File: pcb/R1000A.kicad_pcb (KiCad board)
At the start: 4 copper layers, 175 x 65.5 mm, 120 parts, among them J01 PCIESOCKET-X1, J02 PCIESOCKET-X1, J03 PCIESOCKET-X1, J04 PCIESOCKET-X1, J05 PCIESOCKET-X1, J06 PCIESOCKET-X1, J07 PCIESOCKET-X1, J08 PCIESOCKET-X1, J09 PCIESOCKET-X1, J10 PCIESOCKET-X1, J11 PCIESOCKET-X1, J12 PCIESOCKET-X1, J13 PCIESOCKET-X1, J14 PCIESOCKET-X1, J15 PCIESOCKET-X1, J17 USB_B_RECEPTACLE, J2 CONN127P-02X05, J25 SOCKET420P-02X04-CPU, J27 CONN500P-01X04, J31 USB_A_RECEPTACLE_2, J80 SOCKET254P-01X02, J81 SOCKET254P-01X02, J82 SOCKET254P-01X02, J83 CONN_01X03, Q1 DMG2305UX-7, Q2 PSMN1R2-30YLC, Q3 Q_PNP_BEC, Q4 Q_NPN_BEC, U1 LPC1769FBD100,551, U2 AP3418, U3 BD9E302EFJ-E2, U4 INA3221AIRGVR, U5 LM5060MM/NOPB, Y1 XTAL4_12MHz

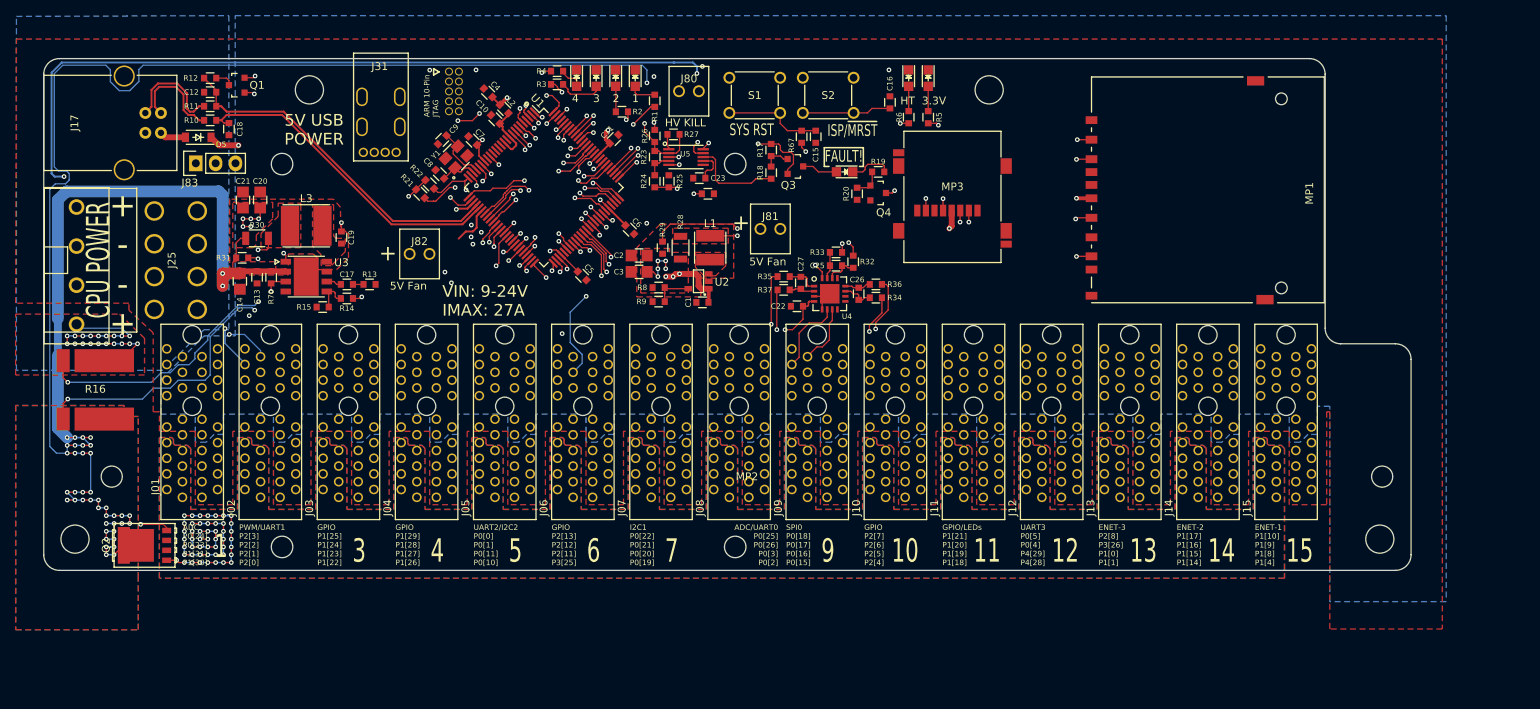
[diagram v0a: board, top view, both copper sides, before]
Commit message: added fiducials and re-laid ground and high tension planes
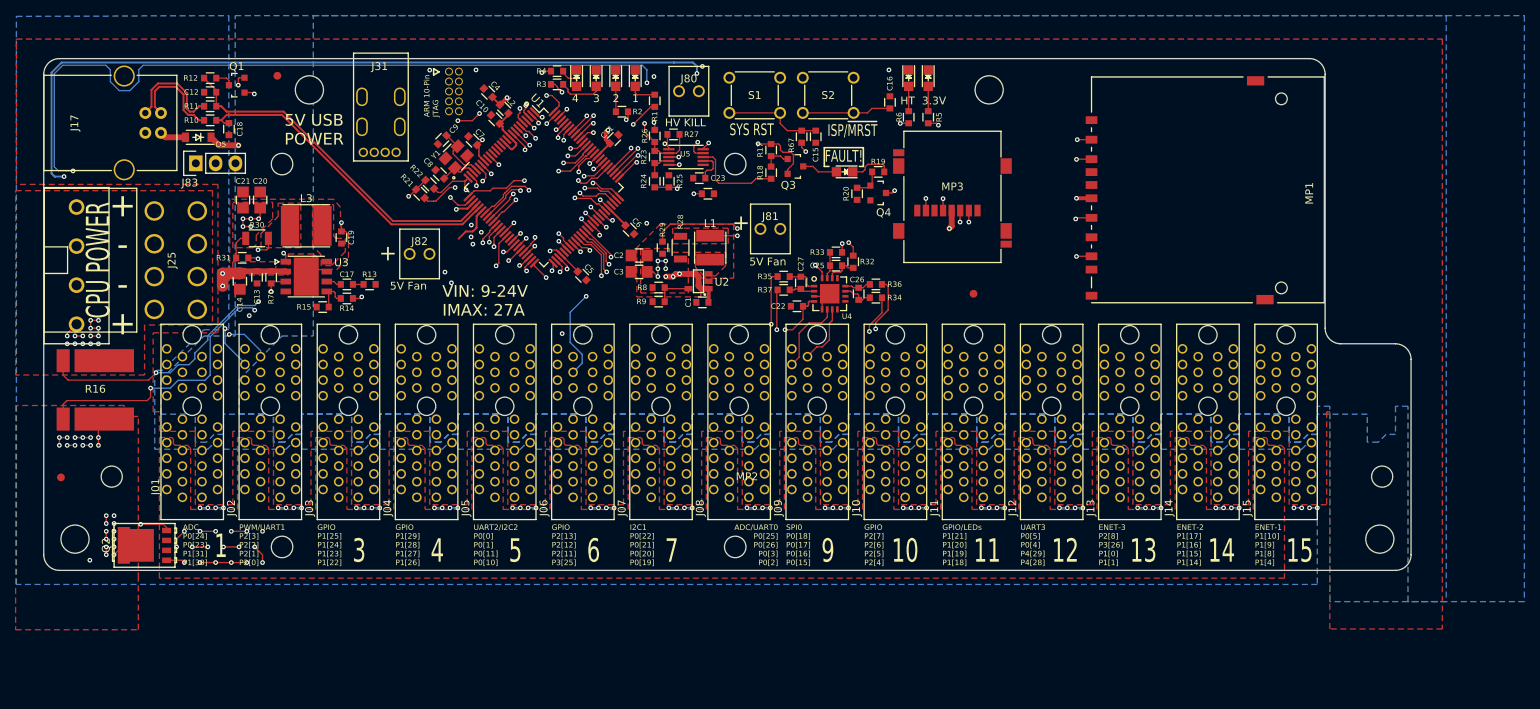
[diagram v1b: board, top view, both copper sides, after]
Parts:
- added FID1: FIDTOP001, Main:FIDTOP001, F.Cu at (80.9, 75.7)
- added FID2: FIDTOP001, Main:FIDTOP001, F.Cu at (53.2, 127.1)
- added FID3: FIDTOP001, Main:FIDTOP001, F.Cu at (170.0, 103.6)
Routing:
- net GND: track 15.0 -> 159.5 mm, vias 0 -> 60
- net PFET_D: track 306.1 -> 248.2 mm, vias 44 -> 30
- net HT_IN: track 32.2 -> 19.4 mm, vias 19 -> 14
- net HT: track 259.4 -> 247.1 mm, vias 54 -> 22
- net /PowerMonitor/IIN-: track 120.9 -> 121.5 mm
- net /PowerMonitor/LM5060_GATE: track 189.1 -> 189.3 mm, vias 4 -> 5
- added copper zone on B.Cu, net GND
- added copper zone on In1.Cu, net HT_IN
- removed copper zone on B.Cu, net HT
- removed copper zone on In2.Cu, net HT
- removed copper zone on B.Cu, net HT_IN
- removed copper zone on In2.Cu, net HT_IN
- removed copper zone on B.Cu, net PFET_D
- removed copper zone on In2.Cu, net PFET_D

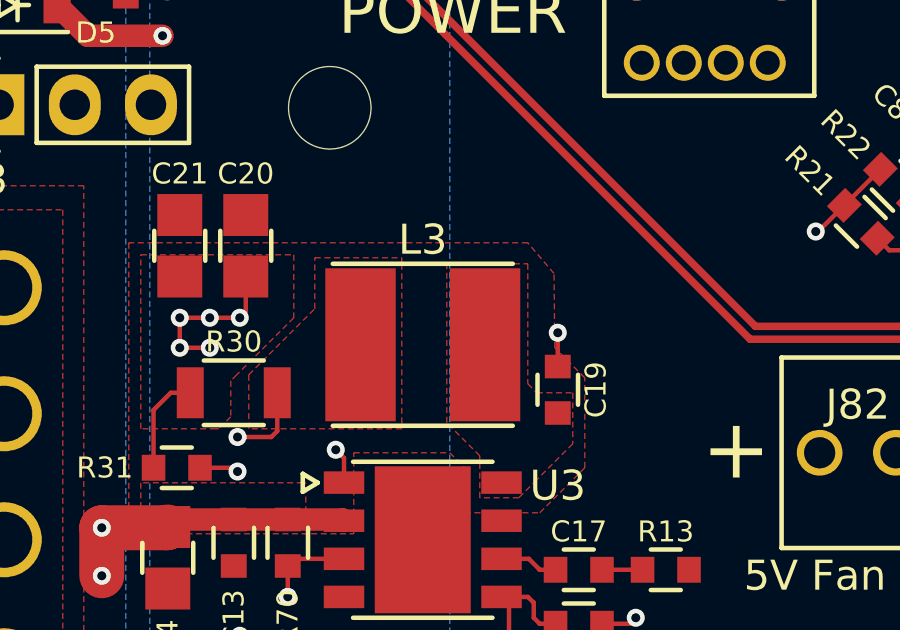
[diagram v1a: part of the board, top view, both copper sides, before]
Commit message: fixed dfm orientation for L3
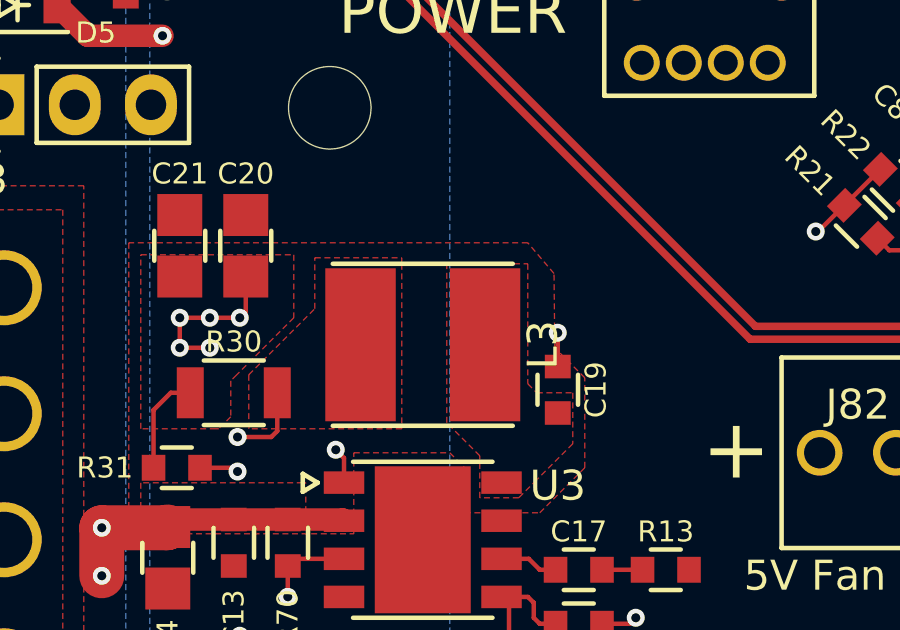
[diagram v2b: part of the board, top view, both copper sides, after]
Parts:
- turned L3 to 270 degrees
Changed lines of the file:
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@@
     (links 716)
     (no_connects 0)
-    (area 50.924999 73.424999 226.075001 139.075001)
+    (area 47.4 63.678571 240.500001 147.400001)
     (thickness 1.6)
     (drawings 71)
@@
   (page A4)
   (layers
-    (0 F.Cu signal hide)
+    (0 F.Cu signal)
     (1 In1.Cu signal hide)
-    (2 In2.Cu signal)
+    (2 In2.Cu signal hide)
     (31 B.Cu signal hide)
     (32 B.Adhes user)
@@
     )
   )
-  (module Main:INDP600600X420 (layer F.Cu)
-    (at 84.6 94.9 180)
-    (fp_text reference L3 (at 0 3.5 180) (layer F.SilkS)
-      (effects (font (size 1 1) (thickness 0.15)))
-    )
-    (fp_text value INDUCTOR_SRN6045TA-4R7M (at 0 -0.5 180) (layer F.Fab) hide
-      (effects (font (size 0.127 0.127) (thickness 0.03)))
-    )
-    (fp_line (start 3.3 2.8) (end -3.3 2.8) (layer F.CrtYd) (width 0.1524))
-    (fp_line (start -3.3 2.8) (end -3.3 -2.8) (layer F.CrtYd) (width 0.1524))
-    (fp_line (start -3.3 -2.8) (end 3.3 -2.8) (layer F.CrtYd) (width 0.1524))
-    (fp_line (start 3.3 -2.8) (end 3.3 2.8) (layer F.CrtYd) (width 0.1524))
-    (fp_line (start 3 2.7) (end -3 2.7) (layer F.SilkS) (width 0.1524))
-    (fp_line (start 3 -2.7) (end -3 -2.7) (layer F.SilkS) (width 0.1524))
-    (pad 1 smd rect (at -2.075 0 180) (size 2.35 5.1) (layers F.Cu F.Paste F.Mask)
-      (net 89 /Power/SW5V0))
-    (pad 2 smd rect (at 2.075 0 180) (size 2.35 5.1) (layers F.Cu F.Paste F.Mask)
-      (net 124 5V0+))
-    (model main.3dshapes/INDP600600X420.wrl
-      (at (xyz 0 0 0))
-      (scale (xyz 1 1 1))
-      (rotate (xyz 0 0 0))
-    )
-  )
   (module Main:CONN_SCHD3A0100 (layer F.Cu)
     (at 167.3 82.8)
@@
       (solder_mask_margin 0.77) (clearance 0.77))
   )
+  (module Main:INDP600600X420 (layer F.Cu)
+    (at 84.6 94.9 270)
+    (fp_text reference L3 (at 0 -4 270) (layer F.SilkS)
+      (effects (font (size 1 1) (thickness 0.15)))
+    )
+    (fp_text value INDUCTOR_SRN6045TA-4R7M (at 0 -0.5 270) (layer F.Fab) hide
+      (effects (font (size 0.127 0.127) (thickness 0.03)))
+    )
+    (fp_line (start 2.8 3.3) (end 2.8 -3.3) (layer F.CrtYd) (width 0.1524))
+    (fp_line (start 2.8 -3.3) (end -2.8 -3.3) (layer F.CrtYd) (width 0.1524))
+    (fp_line (start -2.8 -3.3) (end -2.8 3.3) (layer F.CrtYd) (width 0.1524))
+    (fp_line (start -2.8 3.3) (end 2.8 3.3) (layer F.CrtYd) (width 0.1524))
+    (fp_line (start 2.7 3) (end 2.7 -3) (layer F.SilkS) (width 0.1524))
+    (fp_line (start -2.7 3) (end -2.7 -3) (layer F.SilkS) (width 0.1524))
+    (pad 1 smd rect (at 0 -2.075 270) (size 5.1 2.35) (layers F.Cu F.Paste F.Mask)
+      (net 89 /Power/SW5V0))
+    (pad 2 smd rect (at 0 2.075 270) (size 5.1 2.35) (layers F.Cu F.Paste F.Mask)
+      (net 124 5V0+))
+    (model main.3dshapes/INDP600600X420.wrl
+      (at (xyz 0 0 0))
+      (scale (xyz 1 1 1))
+      (rotate (xyz 0 0 0))
+    )
+  )
   (gr_text "HV KILL" (at 130.5 81.7) (layer F.SilkS)

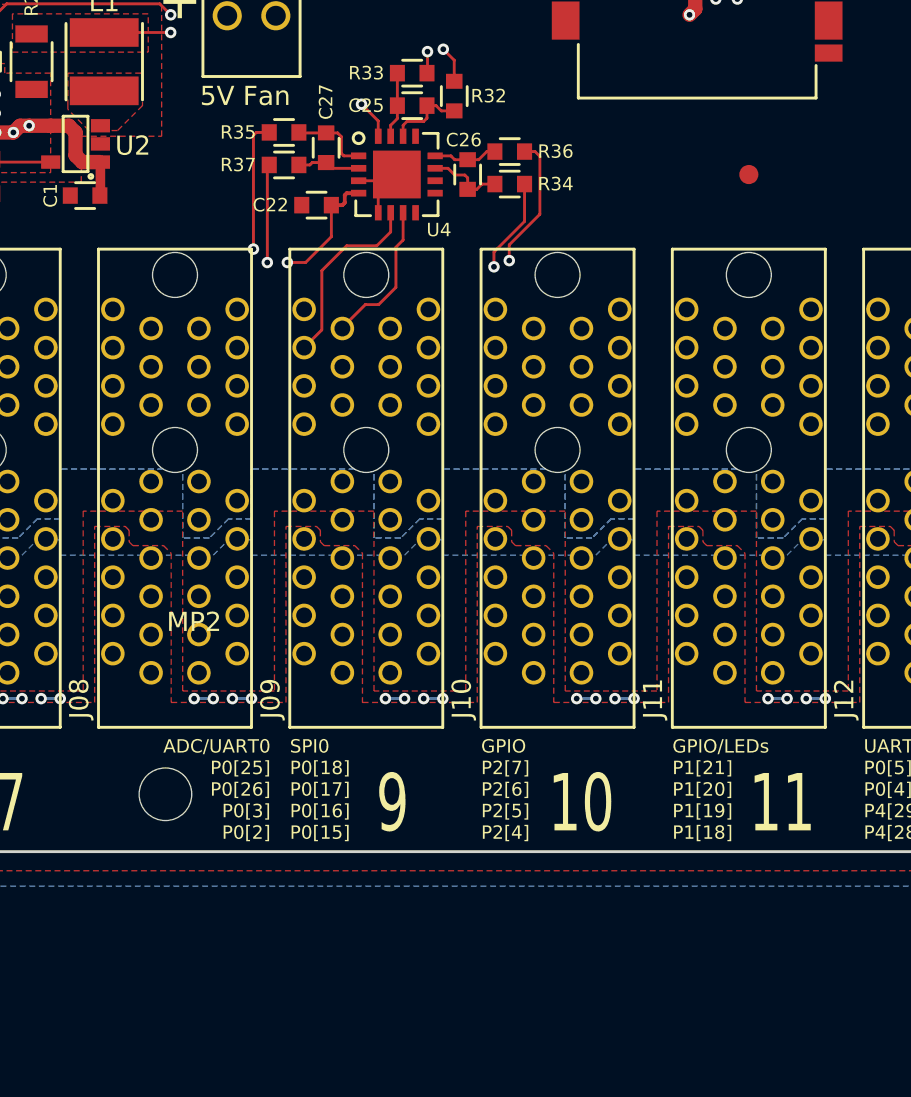
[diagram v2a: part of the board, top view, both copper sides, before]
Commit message: wip, added eeprom and test point for write protecting ROM during normal operation
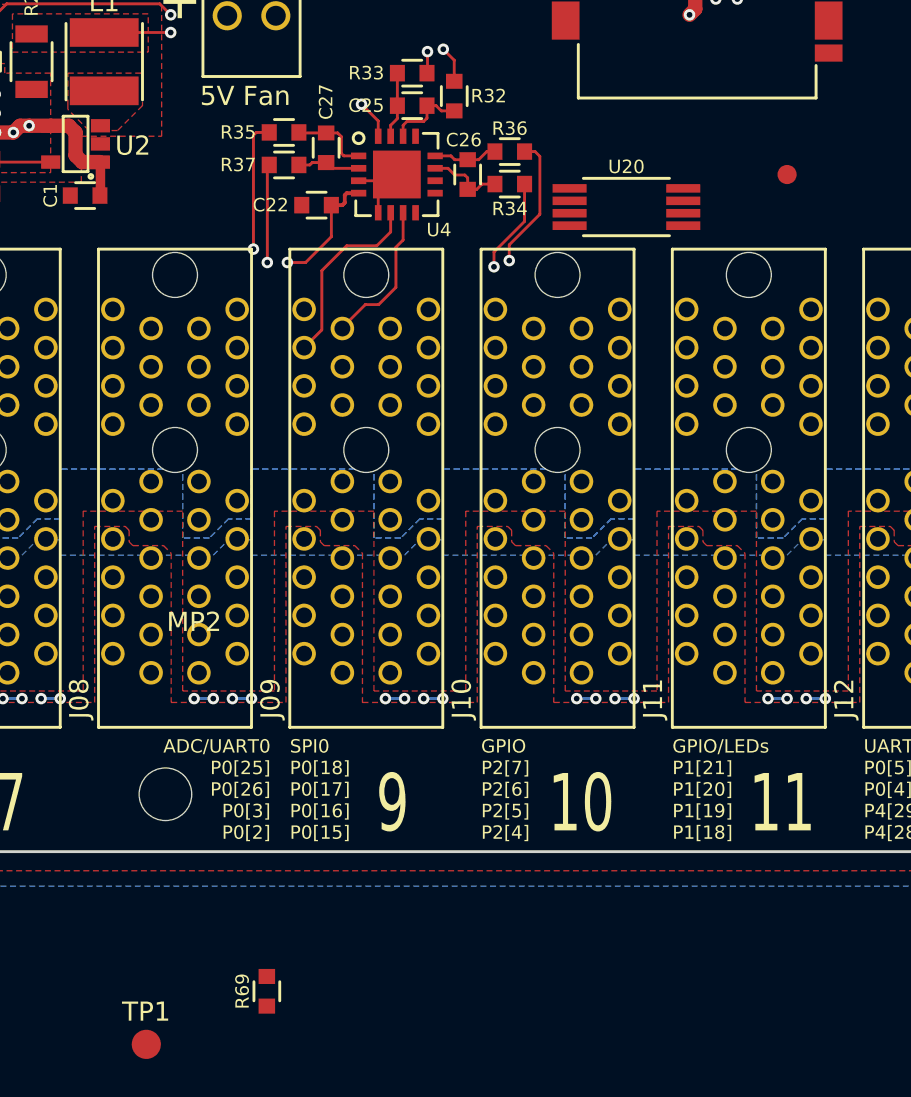
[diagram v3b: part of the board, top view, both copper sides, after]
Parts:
- added R69: R0603, Main:RESC0603, F.Cu at (144.8, 146.3)
- added TP1: TestPoint, Main:TestPoint000, F.Cu at (138.5, 149.1)
- added U20: M24C08-WDW6TP, Main:SOP65P440X300X120-8, F.Cu at (163.6, 105.3)
- moved FID3 2.00 mm to (172.0, 103.6)

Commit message: wip, adding eeprom
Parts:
- moved R69 50.5 mm to (157.9, 97.5), turned to 270 degrees
- moved U20 3.11 mm to (163.4, 102.2)
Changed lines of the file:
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@@
     (links 724)
     (no_connects 494)
-    (area 50.924999 73.424999 226.075001 139.075001)
+    (area 47.4 63.678571 240.500001 150.660001)
     (thickness 1.6)
     (drawings 71)
@@
     (0 F.Cu signal)
     (1 In1.Cu signal)
-    (2 In2.Cu signal)
+    (2 In2.Cu signal hide)
     (31 B.Cu signal hide)
     (32 B.Adhes user)
@@
   )
   (module Main:RESC0603 (layer F.Cu)
-    (at 144.8 146.3 90)
+    (at 157.9 97.5 270)
     (descr "Resistor SMD 0603, reflow soldering, Vishay (see dcrcw.pdf)")
     (tags "resistor 0603")
     (attr smd)
-    (fp_text reference R69 (at 0 -1.27 90) (layer F.SilkS)
+    (fp_text reference R69 (at 0 -1.27 270) (layer F.SilkS)
       (effects (font (size 0.7 0.7) (thickness 0.15)))
     )
-    (fp_text value R0603 (at 0 0.508 90) (layer F.Fab)
+    (fp_text value R0603 (at 0 0.508 270) (layer F.Fab)
       (effects (font (size 0.127 0.127) (thickness 0.03)))
     )
@@
     (fp_line (start 0.5 0.675) (end -0.5 0.675) (layer F.SilkS) (width 0.15))
     (fp_line (start -0.5 -0.675) (end 0.5 -0.675) (layer F.SilkS) (width 0.15))
-    (pad 1 smd rect (at -0.7745 0 90) (size 0.787 0.864) (layers F.Cu F.Paste F.Mask)
+    (pad 1 smd rect (at -0.7745 0 270) (size 0.787 0.864) (layers F.Cu F.Paste F.Mask)
       (net 2 GND))
-    (pad 2 smd rect (at 0.7745 0 90) (size 0.787 0.864) (layers F.Cu F.Paste F.Mask)
+    (pad 2 smd rect (at 0.7745 0 270) (size 0.787 0.864) (layers F.Cu F.Paste F.Mask)
       (net 129 "Net-(R69-Pad2)"))
     (model main.3dshapes/RESC0603.wrl
@@
   )
   (module Main:SOP65P440X300X120-8 (layer F.Cu)
-    (at 163.6 105.3 90)
-    (fp_text reference U20 (at 2.1 0 180) (layer F.SilkS)
+    (at 163.4 102.2 90)
+    (fp_text reference U20 (at -2.3 0 180) (layer F.SilkS)
       (effects (font (size 0.7 0.7) (thickness 0.15)))
     )

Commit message: wip, tagging
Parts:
- removed J27: CONN500P-01X04, Main:CONN500P-01X04
- removed J80: SOCKET254P-01X02, Main:SOCKET254P-01X02
- removed MP5: RPi_Mount, Main:DOCK_RPI_NO_SLKSCRN
- added Q5: Q_PNP_BEC, Main:SOT190P290X130X100-3, F.Cu at (132.0, 151.0)
- added Q6: Q_PNP_BEC, Main:SOT190P290X130X100-3, F.Cu at (144.0, 152.0)
- added R38: RC0603FR-072K21L, Main:RESC0603, F.Cu at (139.0, 150.0)
- added R7: RC0603FR-0710KL, Main:RESC0603, F.Cu at (138.0, 154.0)
- C1: value C0603 -> CC0603KRX5R5BB475
- C10, C11, C13, C19, C22, C25, C26, C27, C4, C5, C6, C7: value C0603 -> CC0603KRX7R9BB104
- C12, C18: value C0603 -> CC0603JRNPO9BN180
- C14: value C0805 -> CL21A475KLCLQNC
- C15, C16, C24: value C0603 -> CC0603KRX7R9BB103
- C17: value C0603 -> CC0603KRX7R9BB682
- C2, C20, C21, C3: value C0805 -> CC0805MKX5R5BB226
- C23: value C0603 -> CC0603JRNPO9BN102
- C8, C9: value C0603 -> CC0603JRNPO9BN120
- R1, R2, R3, R4, R5: value R0603 -> RC0603FR-071KL
- R10, R11: value R0603 -> RC0603FR-0733R2L
- R12: value R0603 -> RC0603FR-071K5L
- R13, R17, R18, R19, R20, R21, R22, R67, R69: value R0603 -> RC0603FR-0710KL
- R14: value R0603 -> RC0603FR-0751K1L
- R15: value R0603 -> RC0603FR-079K76L
- R23, R26, R70: value R0603 -> RC0603FR-0766K5L
- R24: value R0603 -> RC0603FR-0711KL
- R25: value R0603 -> RC0603FR-076K49L
- R27, R6: value R0603 -> RC0603FR-072K21L
- R28, R30: value R1206 -> ERJ-8CWFR030V
- R29, R31: value R0603 -> RC0603FR-070RL
- R32, R33, R34, R35, R36, R37: value R0603 -> RC0603FR-077R5L
- R8: value R0603 -> RC0603FR-0727K4L
- R9: value R0603 -> RC0603FR-076K04L
- TP1: moved to B.Cu
- moved TP1 54.2 mm to (159.2, 99.0)
- moved R17 6.00 mm to (138.1, 85.2)
- moved R18 4.80 mm to (139.3, 88.3)
- moved R69 2.52 mm to (159.3, 99.6)
- moved R34 2.40 mm to (155.8, 105.8)
- moved U20 1.80 mm to (162.4, 103.7), turned to 270 degrees
- moved R36 1.30 mm to (157.0, 103.6), turned to 270 degrees
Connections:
- C13 pad 1: PFET_D -> HT
- C14 pad 1: PFET_D -> HT
- Q3 pad 3: Net-(DLED5-Pad2) -> Net-(Q3-Pad3)
- R19 pad 1: Net-(DLED5-Pad1) -> Net-(Q3-Pad3)
- R70 pad 1: PFET_D -> HT
- U3 pad 2: PFET_D -> HT
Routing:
- net PFET_D: track 248.2 -> 20.5 mm, vias 30 -> 1
- net HT: track 247.1 -> 390.2 mm, vias 22 -> 26
- net GND: track 159.5 -> 189.5 mm, vias 60 -> 82
- net HT_IN: track 19.4 -> 3.72 mm, vias 14 -> 0
- net (no net): track 0.00 -> 15.7 mm, vias 0 -> 14
- net SCL0: track 239.2 -> 253.9 mm
- net CHIP_~PGD: track 11.8 -> 0.00 mm
- net Net-(R69-Pad2): track 0.00 -> 11.5 mm, vias 0 -> 1
- net SDA0: track 217.8 -> 228.9 mm
- net Net-(DLED5-Pad1): track 5.46 -> 0.00 mm
- net Net-(DLED5-Pad2): track 4.54 -> 0.00 mm
- net Net-(Q3-Pad1): track 3.61 -> 0.00 mm
- net HV_EN: track 147.1 -> 143.7 mm
- net /PowerMonitor/IIN+: track 121.7 -> 118.7 mm
- net /PowerMonitor/IIN-: track 121.5 -> 119.2 mm
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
